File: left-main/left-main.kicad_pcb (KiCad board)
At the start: 2 copper layers, 136 x 123.8 mm, 205 parts, among them P1 CONN_4, P2 CONN_5, P3 CONN_6, P4 CONN_18, Q1 PNP, Q2 PNP, SW11 SPST, SW12 SPST, SW13 SPST, SW14 SPST, SW15 SPST, SW16 SPST, SW17 SPST, SW21 SPST, SW22 SPST, SW23 SPST, SW24 SPST, SW25 SPST, SW27 SPST, SW31 SPST, SW32 SPST, SW33 SPST, SW34 SPST, SW35 SPST, SW37 SPST, SW411 SPST, SW412 SPST, SW42 SPST, SW43 SPST, SW44 SPST, SW45 SPST, SW46 SPST, SW47 SPST, SW51 SPST, SW52 SPST, SW53 SPST, SW54 SPST, SW55 SPST, SW56 SPST, U1 ATMEGA88, U2 PCA9634, U3 TPIC6C595, X1 16Mhz

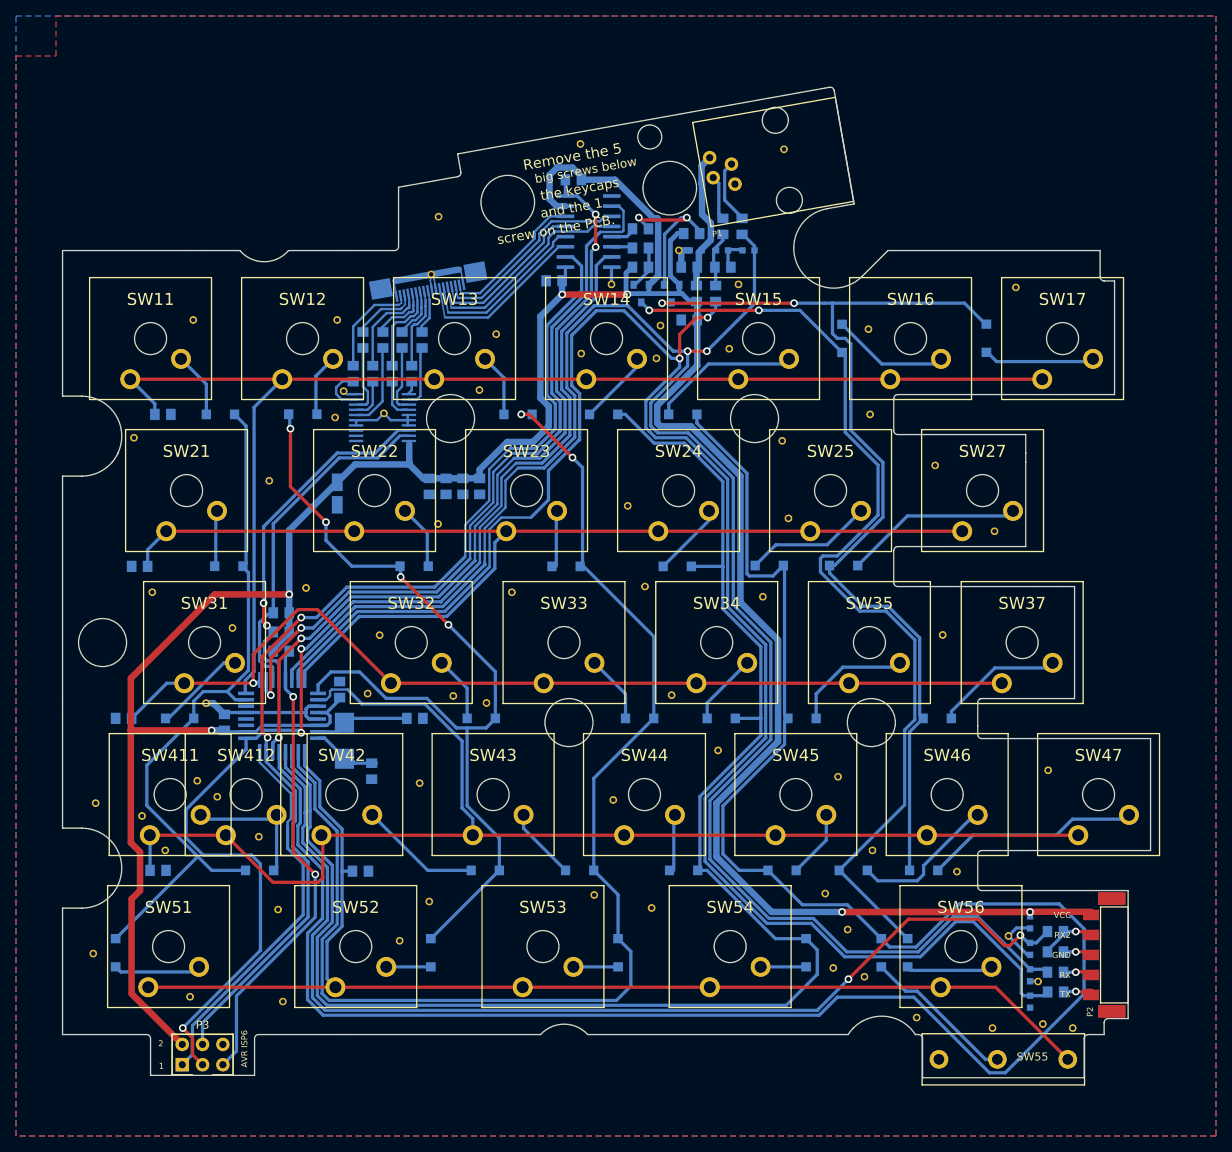
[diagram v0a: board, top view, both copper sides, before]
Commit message: Replaces a lot of switches with hybrid switches
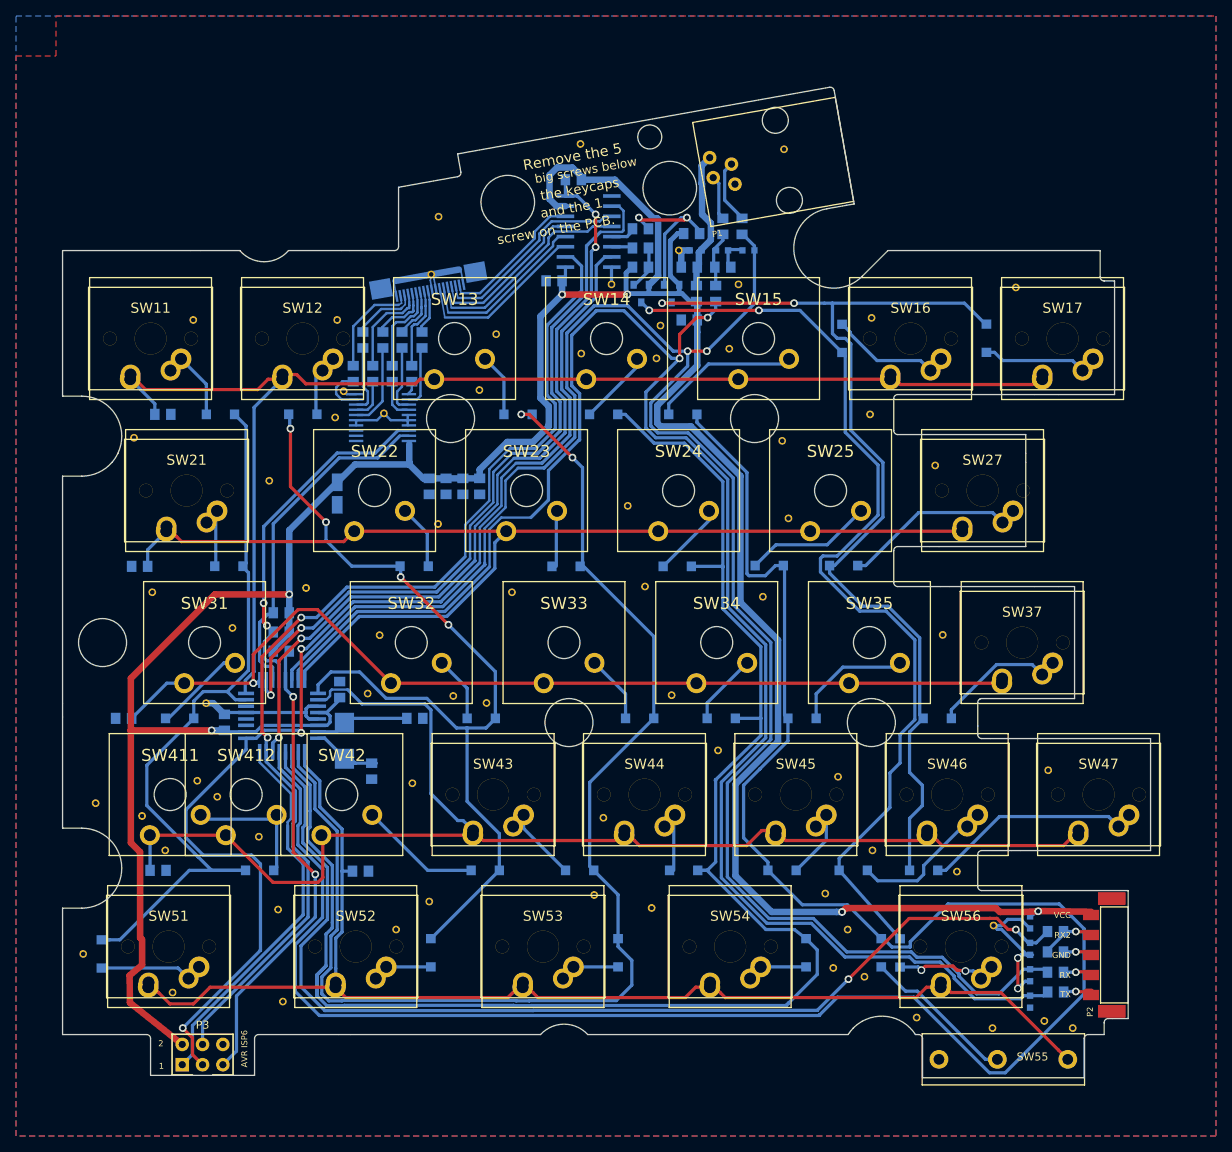
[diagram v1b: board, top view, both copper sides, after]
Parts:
- SW11, SW12, SW16, SW17, SW21, SW27, SW37, SW43, SW44, SW45, SW46, SW47, SW51, SW52, SW53, SW54, SW56: footprint UGL:Cherry_MX -> ugl:Cherry-MX-Matias-Hybrid
- U1: value ATMEGA88 -> ATMEGA88-A
- moved via 38/22mil 2.55 mm to (193.4, 125.2)
- moved via 35/25mil 2.28 mm to (242.2, 138.7)
- moved via 38/22mil 2.25 mm to (139.6, 147.1)
- moved D51 1.78 mm to (130.7, 142.2)
- moved via 38/22mil 1.47 mm to (167.5, 139.2)
- moved via 38/22mil 1.46 mm to (226.9, 62.7)
- moved via 38/22mil 1.26 mm to (128.4, 142.2)
- moved D56 0.95 mm to (230.5, 142.1)
- moved via 38/22mil 0.91 mm to (169.5, 120.9)
- moved via 38/22mil 0.42 mm to (248.5, 150.6)
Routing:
- net GND: track 65.5 -> 77.3 mm, vias 1 -> 3
- net /KEYS_COL1: track 90.0 -> 97.1 mm
- net /TX: track 225.4 -> 218.8 mm
- net /KEYS_COL4: track 197.8 -> 203.6 mm
- net /KEYS_ROW5: track 152.7 -> 157.3 mm
- net /KEYS_ROW4: track 163.7 -> 167.6 mm
- net Net-(D51-Pad2): track 11.0 -> 14.3 mm
- net /KEYS_ROW1: track 161.0 -> 164.0 mm
- net /RX: track 234.4 -> 231.7 mm
- net /KEYS_COL5: track 270.0 -> 267.8 mm
- net Net-(D27-Pad2): track 24.3 -> 26.3 mm
- net Net-(D53-Pad2): track 5.58 -> 7.59 mm
- net Net-(D52-Pad2): track 5.58 -> 7.58 mm
- net Net-(D45-Pad2): track 8.60 -> 10.6 mm
- net Net-(D43-Pad2): track 9.11 -> 11.1 mm
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
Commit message: Adds most matias keys
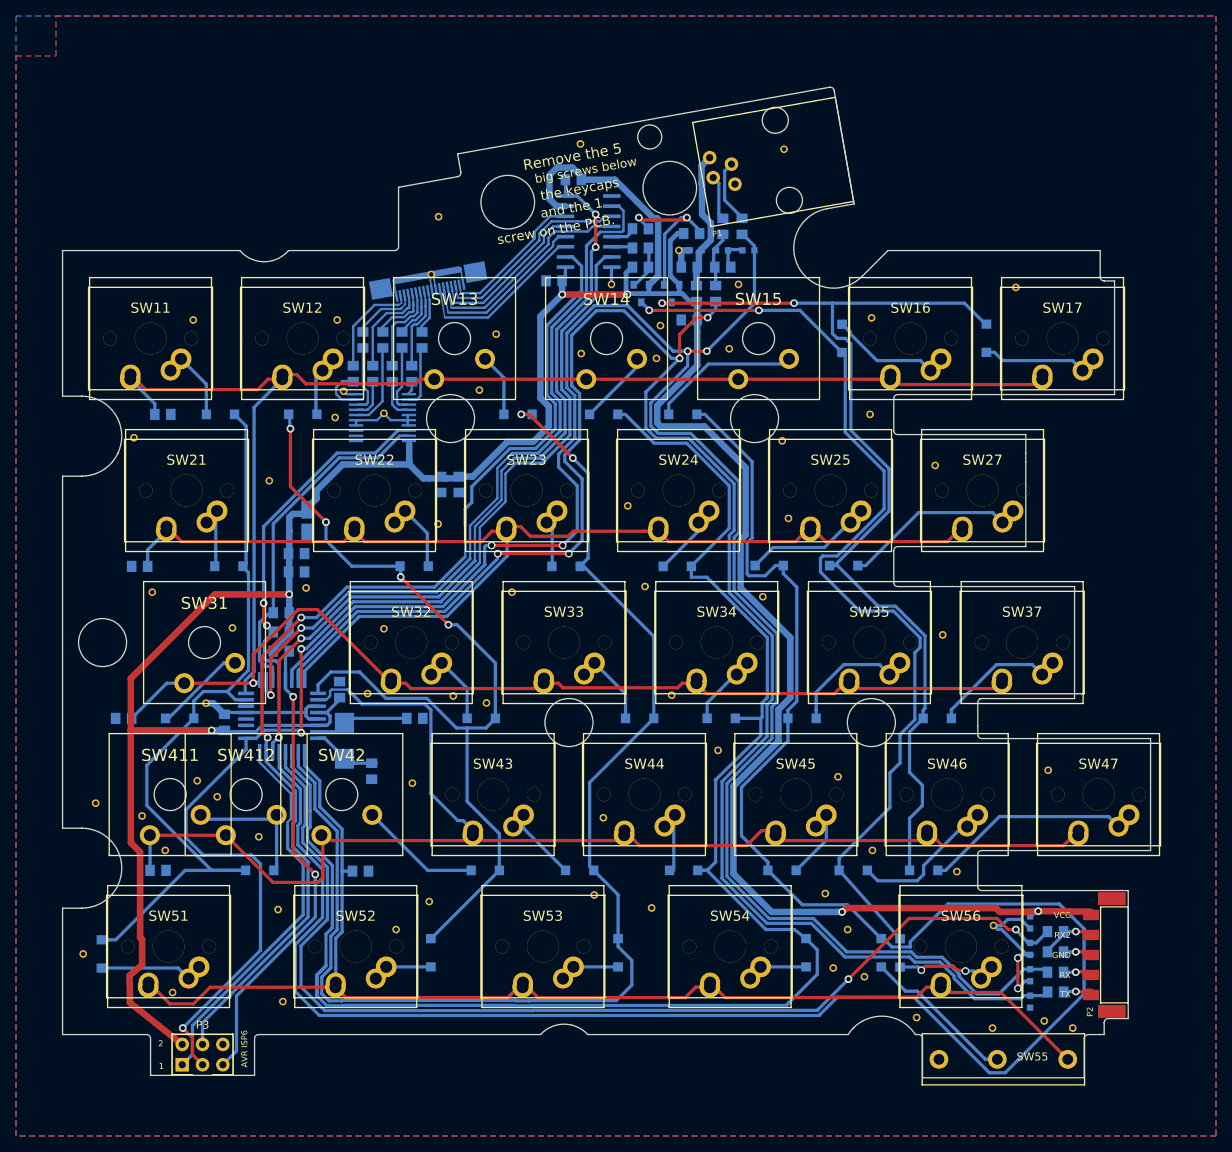
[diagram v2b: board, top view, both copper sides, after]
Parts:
- SW22, SW23, SW24, SW25, SW32, SW33, SW34, SW35: footprint UGL:Cherry_MX -> ugl:Cherry-MX-Matias-Hybrid
- SW42: footprint UGL:Cherry_MX -> ugl:Cherry_MX
- moved C12 21.5 mm to (155.1, 94.5), turned to 180 degrees
- moved C13 18.6 mm to (155.1, 92.2), turned to 180 degrees
- moved C14 5.14 mm to (156.3, 88.1)
- moved C11 2.77 mm to (173.1, 83.6)
- moved C10 2.58 mm to (175.4, 83.6)
- moved via 35/25mil 0.96 mm to (166.0, 101.6)
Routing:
- net VCC: track 381.1 -> 393.4 mm
- net /RX: track 231.7 -> 238.7 mm, vias 2 -> 4
- net /TX: track 218.8 -> 224.9 mm, vias 2 -> 4
- net /KEYS_ROW2: track 141.6 -> 146.6 mm
- net /KEYS_ROW3: track 121.3 -> 125.0 mm
- net /KEYS_COL5: track 267.8 -> 270.0 mm
- net Net-(D44-Pad2): track 7.00 -> 9.00 mm
- net Net-(D34-Pad2): track 9.27 -> 11.3 mm
- net Net-(D24-Pad2): track 9.58 -> 11.6 mm
- net Net-(D22-Pad2): track 8.07 -> 10.1 mm
- net Net-(D33-Pad2): track 8.54 -> 10.5 mm
- net Net-(D32-Pad2): track 8.27 -> 10.3 mm
- net Net-(D25-Pad2): track 16.1 -> 18.1 mm
- net /KEYS_COL4: track 203.6 -> 205.4 mm
- net /KEYS_COL6: track 120.7 -> 122.5 mm
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
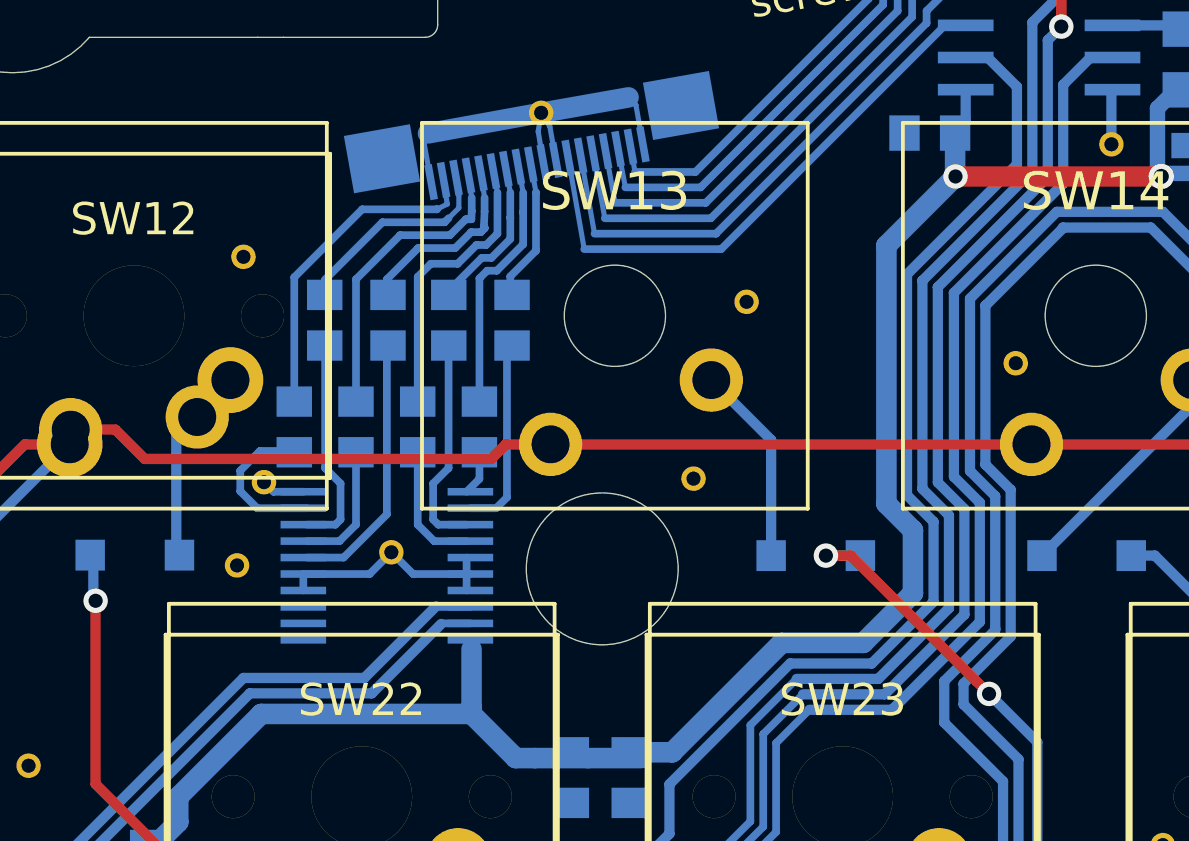
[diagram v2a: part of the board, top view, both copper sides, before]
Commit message: switch 12 and 13 resistors moved
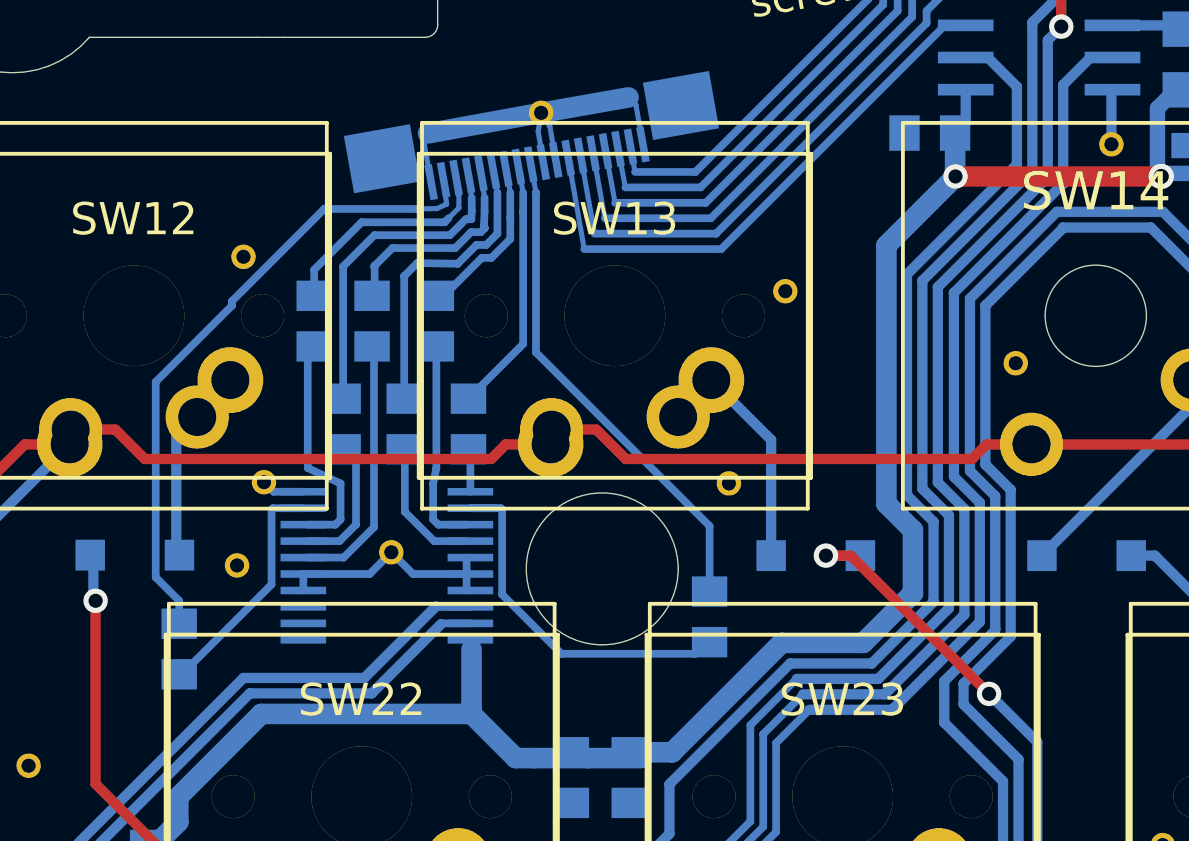
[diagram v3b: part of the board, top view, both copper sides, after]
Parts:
- SW13: footprint UGL:Cherry_MX -> ugl:Cherry-MX-Matias-Hybrid
- moved R28 14.1 mm to (178.6, 77.2)
- moved R21 9.88 mm to (157.6, 78.5)
- moved via 38/22mil 1.41 mm to (179.3, 71.9)
- moved R24 0.63 mm to (165.2, 65.5)
- moved R25 0.55 mm to (166.5, 69.6)
- moved R23 0.52 mm to (164.1, 69.6)
- moved R26 0.49 mm to (167.8, 65.5)
- moved R27 0.45 mm to (169.0, 69.6)
- moved R22 0.42 mm to (162.9, 65.5)
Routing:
- net /LEDS_COL8: track 5.95 -> 19.7 mm
- net /LEDS_COL1: track 13.1 -> 25.5 mm
- net /LEDS_R8: track 7.32 -> 15.0 mm
- net /LEDS_R1: track 6.19 -> 9.36 mm
- net Net-(D13-Pad2): track 7.91 -> 9.92 mm
- net /LEDS_COL3: track 12.1 -> 12.8 mm
- net /KEYS_ROW1: track 164.0 -> 164.7 mm
- net /LEDS_R2: track 8.23 -> 8.80 mm

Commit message: sw 14
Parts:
- SW14: footprint UGL:Cherry_MX -> ugl:Cherry-MX-Matias-Hybrid
- moved R21 2.34 mm to (156.1, 80.3)
- moved via 38/22mil 1.02 mm to (201.3, 63.0)
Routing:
- net /TX: track 224.9 -> 217.9 mm
- net /LEDS_R1: track 9.36 -> 11.8 mm
- net Net-(D14-Pad2): track 9.39 -> 11.4 mm
- net GND: track 77.3 -> 79.1 mm
- net /LEDS_COL1: track 25.5 -> 27.1 mm
- net /KEYS_ROW1: track 164.7 -> 165.8 mm
- net /RX: track 238.7 -> 237.7 mm
- net VCC: track 393.4 -> 394.0 mm
- net /RCK: track 94.3 -> 94.9 mm
- net /DISPLAY_ENABLE: track 100.5 -> 101.2 mm
- net /MOSI: track 134.9 -> 135.5 mm
- net /SCK: track 149.6 -> 150.3 mm
